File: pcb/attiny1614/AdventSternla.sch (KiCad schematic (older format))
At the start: 15 parts, among them J1 5V In, J2 GPIO_C, J3 UPDI, J4 GPIO_A, J5 NeoPixel, J6 GPIO_A, J7 GPIO_B, U1 ATTINY1614

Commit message: Schematic is done and started the layout
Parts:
- removed C3: 1000μF 16V, symbol CP
- removed J1: 5V In, symbol Conn_01x02_Female
- removed J4: GPIO_A, symbol Conn_01x03_Female
- removed J5: NeoPixel, symbol Conn_01x03_Male
- added C1: 2200μF 25V, Capacitors_ThroughHole:CP_Radial_D13.0mm_P5.00mm, symbol CP
- added J1: 5V In, Pin_Headers:Pin_Header_Straight_1x03_Pitch2.54mm, symbol Jack-DC
- added J6: NeoPixel Data, Pin_Headers:Pin_Header_Straight_1x02_Pitch2.54mm, symbol Conn_01x02_Male
- added J7: Power Out, Pin_Headers:Pin_Header_Straight_1x02_Pitch2.54mm, symbol Conn_01x02_Male
- C2: renamed from C1; footprint 0805 -> Capacitors_SMD:C_0805_HandSoldering
- C3: renamed from C2; footprint (none) -> Capacitors_SMD:C_0805_HandSoldering
- D1: value 5V Zener -> 5V6 Zener; footprint DO-214AA -> Diodes_SMD:D_SOT-23_ANK; Link https://www.reichelt.de/Ueberspannungs-schutzdioden/P6SMB-5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 -> https://www.digikey.de/scripts/DkSearch/dksus.dll?Detail&it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; MPN P6SMB 5,0A SMD -> BZX84-A5V6,215
- J2: footprint (none) -> Pin_Headers:Pin_Header_Straight_1x04_Pitch2.54mm
- J3: footprint (none) -> Pin_Headers:Pin_Header_Straight_2x03_Pitch2.54mm
- J4: renamed from J6; footprint (none) -> Pin_Headers:Pin_Header_Straight_1x03_Pitch2.54mm
- J5: renamed from J7; footprint (none) -> Pin_Headers:Pin_Header_Straight_1x04_Pitch2.54mm
- R1: footprint 1210 -> Resistors_SMD:R_1210_HandSoldering
- R2: footprint 0805 -> Resistors_SMD:R_0805_HandSoldering
- R3: footprint (none) -> Resistors_SMD:R_0805_HandSoldering
- U1: footprint (none) -> SMD_Packages:SOIC-14_N
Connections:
- net 5V: now also C1.1, J1.1, J7.1 (Pin_1)
- net GND: now also C1.2, J1.2, J6.2 (Pin_2), J7.2 (Pin_2)
- net NP_DATA: now reaches R3.2
- net NP_DATA: now also J6.1 (Pin_1)
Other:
- note added: "In System Programming Header - UPDI"
- note added: "The NoePixel has JST \nSM type connnectors"
- note removed: "In System Programming Header"
- moved on the sheet: C2, C3, D1, J2, J3, J4, J5, R1, R2, R3, U1

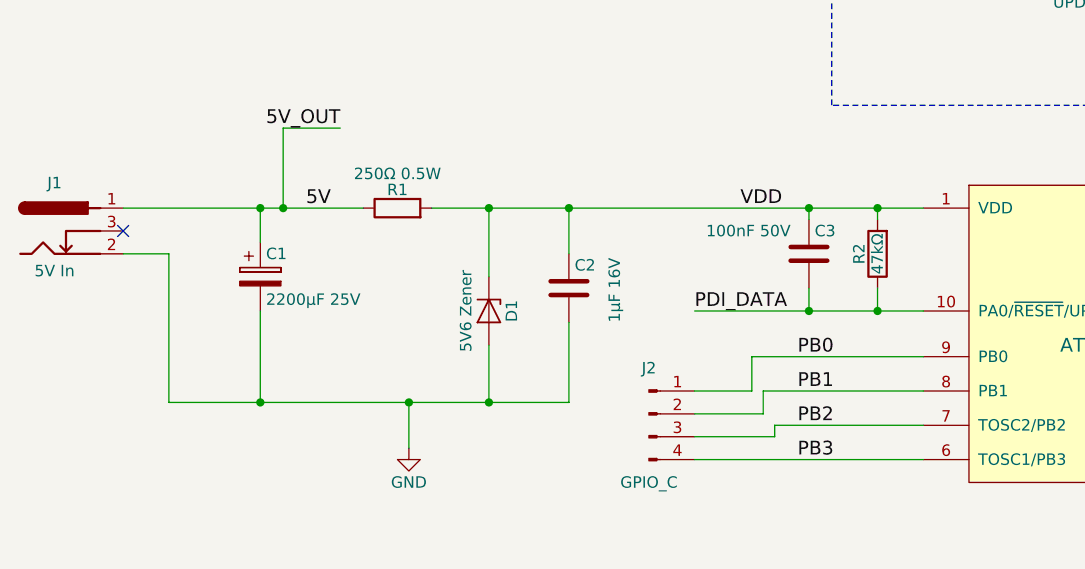
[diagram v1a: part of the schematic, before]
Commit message: Correction to power filtering
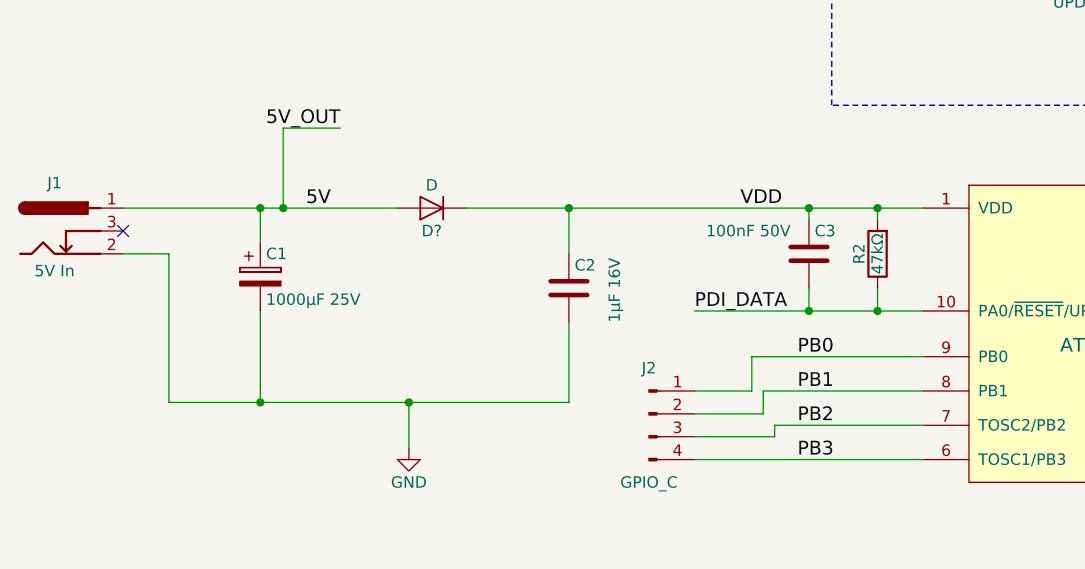
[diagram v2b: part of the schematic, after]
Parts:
- removed D1: 5V6 Zener, Diodes_SMD:D_SOT-23_ANK, symbol D_Zener
- removed R1: 250Ω 0.5W, Resistors_SMD:R_1210_HandSoldering, symbol R
- added D?: D, symbol D
- C1: value 2200μF 25V -> 1000μF 25V
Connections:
- net 5V: now also D?.2 (A)
- net VDD: now also D?.1 (K)
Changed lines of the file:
@@
 PA7
-$Comp
-L D_Zener D1
-U 1 1 59EF89E4
-P 2900 4300
-F 0 "D1" H 2900 4400 50  0000 C CNN
-F 1 "5V6 Zener" H 2900 4200 50  0000 C CNN
-F 2 "Diodes_SMD:D_SOT-23_ANK" H 2900 4300 50  0001 C CNN
-F 3 "http://cdn-reichelt.de/documents/datenblatt/A400/SMBJ_LITTELFUSE_DATASHEET.pdf" H 2900 4300 50  0001 C CNN
-F 4 "BZX84-A5V6,215" H 2900 4300 60  0001 C CNN "MPN"
-F 5 "https://www.digikey.de/scripts/DkSearch/dksus.dll?Detail&itemSeq=242065975&uq=636445409310237522" H 2900 4300 60  0001 C CNN "Link"
-	1    2900 4300
-	0    1    1    0
-$EndComp
-$Comp
-L R R1
-U 1 1 59EF8B11
-P 2500 3850
-F 0 "R1" V 2580 3850 50  0000 C CNN
-F 1 "250Ω 0.5W" V 2650 3850 50  0000 C CNN
-F 2 "Resistors_SMD:R_1210_HandSoldering" V 2430 3850 50  0001 C CNN
-F 3 "" H 2500 3850 50  0001 C CNN
-F 4 "ERJ-14NF2550U" H 2500 3850 60  0001 C CNN "MPN"
-F 5 "https://www.digikey.de/product-detail/de/panasonic-electronic-components/ERJ-14NF2550U/P255AACT-ND/384668" H 2500 3850 60  0001 C CNN "Link"
-	1    2500 3850
-	0    -1   -1   0
-$EndComp
 $Comp
 L Conn_01x04_Male J5
@@
 P 1900 4150
 F 0 "C1" H 1925 4250 50  0000 L CNN
-F 1 "2200μF 25V" H 1925 4050 50  0000 L CNN
+F 1 "1000μF 25V" H 1925 4050 50  0000 L CNN
 F 2 "Capacitors_ThroughHole:CP_Radial_D13.0mm_P5.00mm" H 1938 4000 50  0001 C CNN
 F 3 "" H 1900 4150 50  0001 C CNN
@@
 $EndComp
 Wire Wire Line
-	3800 4300 4800 4300
+	3800 4300 4300 4300
+Wire Wire Line
+	4300 4300 4600 4300
+Wire Wire Line
+	4600 4300 4800 4300
 Wire Wire Line
 	4600 4300 4600 4200
-Wire Wire Line
-	4600 3850 4600 3900
 Wire Wire Line
 	5600 5550 5600 5250
 Connection ~ 4600 4300
-Connection ~ 4600 3850
 Wire Wire Line
 	5200 2650 4750 2650
@@
 	6450 4750 7300 4750
 Wire Wire Line
-	2900 4150 2900 3850
-Wire Wire Line
-	2900 4700 2900 4450
-Wire Wire Line
-	1300 3850 2350 3850
-Wire Wire Line
-	2650 3850 4800 3850
-Connection ~ 2900 3850
+	1300 3850 1900 3850
+Wire Wire Line
+	1900 3850 2000 3850
+Wire Wire Line
+	2000 3850 2500 3850
 Wire Wire Line
 	4100 4650 4800 4650
 Wire Wire Line
 	4800 4950 3800 4950
-Wire Wire Line
-	4300 3850 4300 3900
-Connection ~ 4300 3850
 Wire Wire Line
 	4300 4200 4300 4300
@@
 Wire Wire Line
 	3250 3850 3250 4050
-Connection ~ 3250 3850
 Wire Wire Line
 	3250 4700 3250 4350
@@
 	1900 4300 1900 4700
 Wire Wire Line
-	1500 4700 3250 4700
+	1500 4700 1900 4700
+Wire Wire Line
+	1900 4700 2550 4700
+Wire Wire Line
+	2550 4700 3250 4700
 Wire Wire Line
 	2550 4700 2550 4900
 Connection ~ 1900 4700
 Connection ~ 2550 4700
-Connection ~ 2900 4700
 $Comp
 L Jack-DC J1
@@
 Text Notes 8400 2050 0    100  ~ 0
 NeoPixel
+$Comp
+L D D?
+U 1 1 59F5F260
+P 2650 3850
+F 0 "D?" H 2650 3950 50  0000 C CNN
+F 1 "D" H 2650 3750 50  0000 C CNN
+F 2 "" H 2650 3850 50  0001 C CNN
+F 3 "" H 2650 3850 50  0001 C CNN
+	1    2650 3850
+	-1   0    0    1
+$EndComp
+Wire Wire Line
+	2800 3850 3250 3850
+Wire Wire Line
+	3250 3850 4300 3850
+Wire Wire Line
+	4300 3850 4600 3850
+Wire Wire Line
+	4600 3850 4800 3850
+Connection ~ 3250 3850
+Wire Wire Line
+	4300 3900 4300 3850
+Connection ~ 4300 3850
+Wire Wire Line
+	4600 3900 4600 3850
+Connection ~ 4600 3850
 $EndSCHEMATC

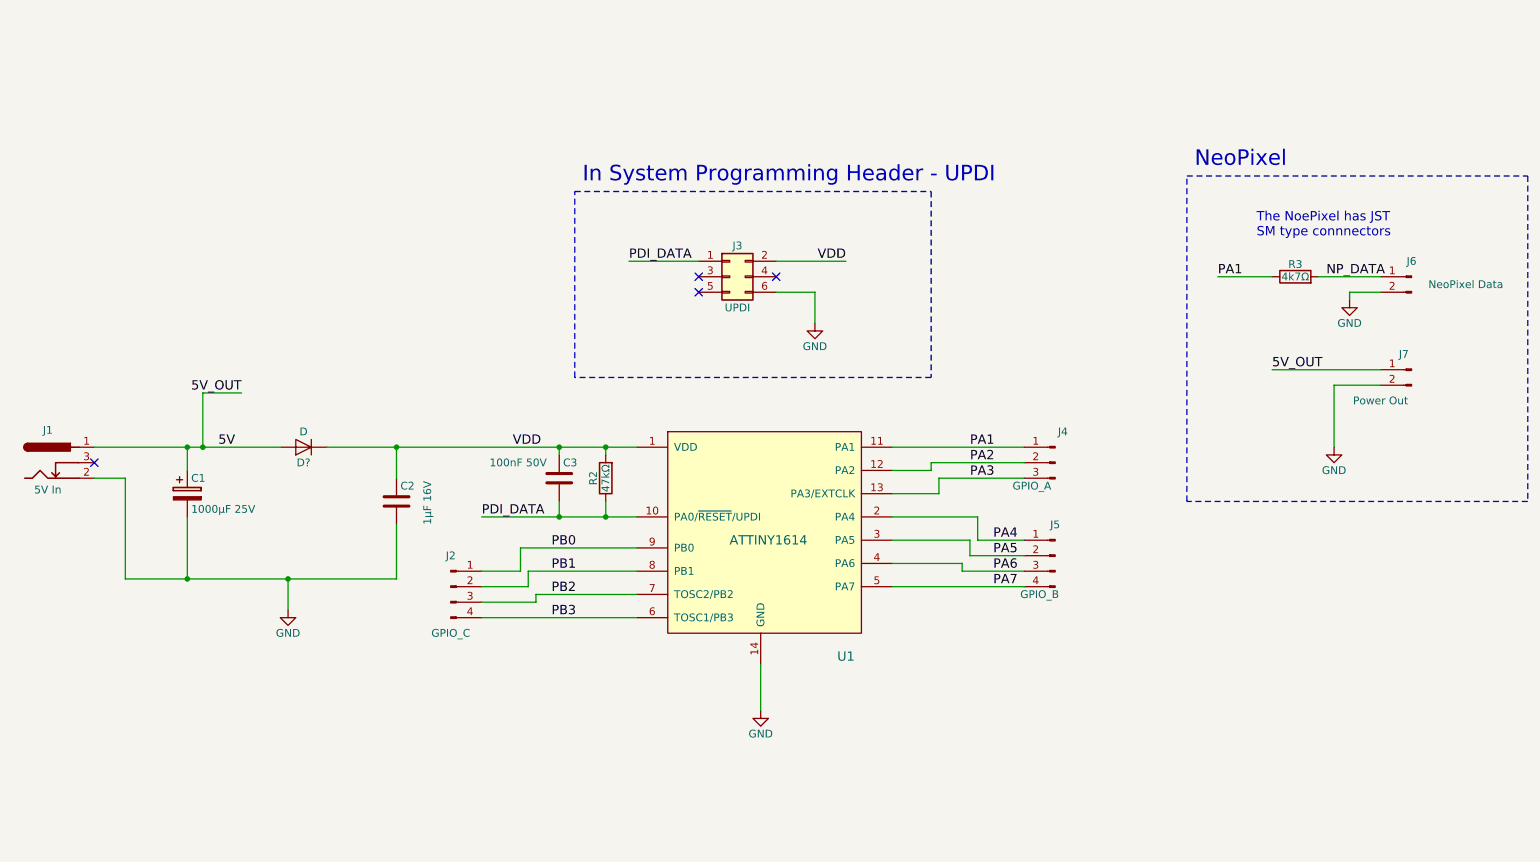
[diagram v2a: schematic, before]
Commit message: Annotated the changes to the power filtering
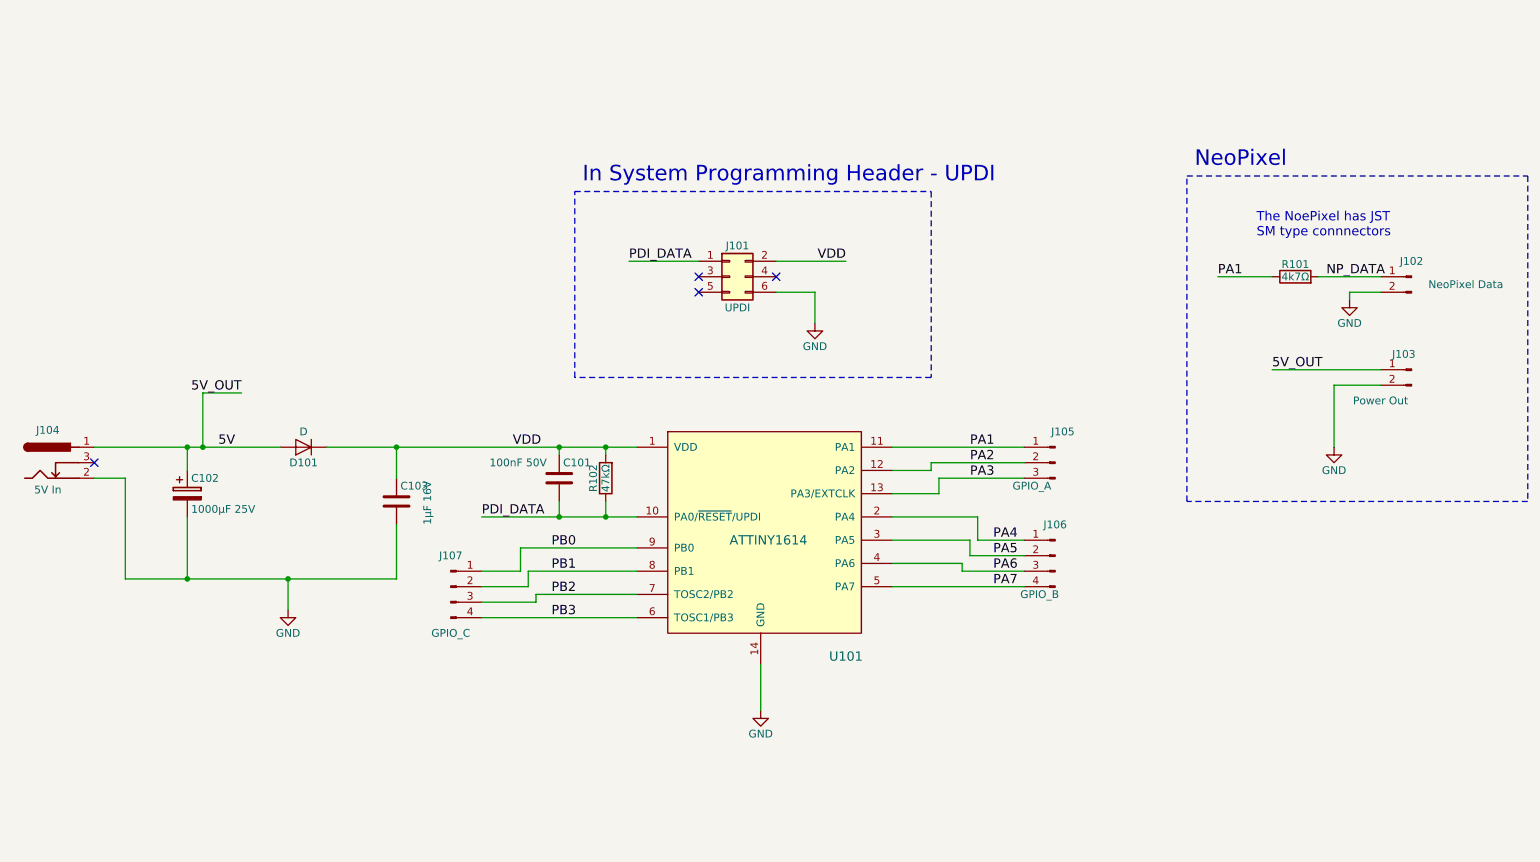
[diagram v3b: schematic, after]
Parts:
- gave numbers to parts that had none: 1
- renumbered C3 to C101, C1 to C102, C2 to C103, J3 to J101, J6 to J102, J7 to J103, J1 to J104, J4 to J105, J5 to J106, J2 to J107, R3 to R101, R2 to R102, U1 to U101
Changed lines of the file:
@@
 $EndDescr
 $Comp
-L ATTINY1614 U1
+L ATTINY1614 U101
 U 1 1 59EF6A42
 P 5600 4400
-F 0 "U1" H 6150 3600 60  0000 C CNN
+F 0 "U101" H 6150 3600 60  0000 C CNN
 F 1 "ATTINY1614" H 5650 4350 60  0000 C CNN
 F 2 "SMD_Packages:SOIC-14_N" H 5450 4450 60  0001 C CNN
@@
 $EndComp
 $Comp
-L R R2
+L R R102
 U 1 1 59EF6A7A
 P 4600 4050
-F 0 "R2" V 4680 4050 50  0000 C CNN
+F 0 "R102" V 4680 4050 50  0000 C CNN
 F 1 "47kΩ" V 4600 4050 50  0000 C CNN
 F 2 "Resistors_SMD:R_0805_HandSoldering" V 4530 4050 50  0001 C CNN
@@
 $EndComp
 $Comp
-L Conn_02x03_Odd_Even J3
+L Conn_02x03_Odd_Even J101
 U 1 1 59EF854F
 P 5400 2750
-F 0 "J3" H 5450 2950 50  0000 C CNN
+F 0 "J101" H 5450 2950 50  0000 C CNN
 F 1 "UPDI" H 5450 2550 50  0000 C CNN
 F 2 "Pin_Headers:Pin_Header_Straight_2x03_Pitch2.54mm" H 5400 2750 50  0001 C CNN
@@
 PA7
 $Comp
-L Conn_01x04_Male J5
+L Conn_01x04_Male J106
 U 1 1 59EF8DC0
 P 7500 4550
-F 0 "J5" H 7500 4750 50  0000 C CNN
+F 0 "J106" H 7500 4750 50  0000 C CNN
 F 1 "GPIO_B" H 7600 4300 50  0000 C CNN
 F 2 "Pin_Headers:Pin_Header_Straight_1x04_Pitch2.54mm" H 7500 4550 50  0001 C CNN
@@
 $EndComp
 $Comp
-L Conn_01x03_Male J4
+L Conn_01x03_Male J105
 U 1 1 59EF8E2B
 P 7500 3950
-F 0 "J4" H 7450 4150 50  0000 C CNN
+F 0 "J105" H 7450 4150 50  0000 C CNN
 F 1 "GPIO_A" H 7650 3800 50  0000 C CNN
 F 2 "Pin_Headers:Pin_Header_Straight_1x03_Pitch2.54mm" H 7500 3950 50  0001 C CNN
@@
 $EndComp
 $Comp
-L Conn_01x04_Male J2
+L Conn_01x04_Male J107
 U 1 1 59EF90A2
 P 3600 4750
-F 0 "J2" H 3600 4950 50  0000 C CNN
+F 0 "J107" H 3600 4950 50  0000 C CNN
 F 1 "GPIO_C" H 3600 4450 50  0000 C CNN
 F 2 "Pin_Headers:Pin_Header_Straight_1x04_Pitch2.54mm" H 3600 4750 50  0001 C CNN
@@
 PB3
 $Comp
-L C C3
+L C C101
 U 1 1 59EF9591
 P 4300 4050
-F 0 "C3" H 4325 4150 50  0000 L CNN
+F 0 "C101" H 4325 4150 50  0000 L CNN
 F 1 "100nF 50V" H 3850 4150 50  0000 L CNN
 F 2 "Capacitors_SMD:C_0805_HandSoldering" H 4338 3900 50  0001 C CNN
@@
 $EndComp
 $Comp
-L C C2
+L C C103
 U 1 1 59EF980D
 P 3250 4200
-F 0 "C2" H 3275 4300 50  0000 L CNN
+F 0 "C103" H 3275 4300 50  0000 L CNN
 F 1 "1μF 16V" V 3450 4050 50  0000 L CNN
 F 2 "Capacitors_SMD:C_0805_HandSoldering" H 3288 4050 50  0001 C CNN
@@
 $EndComp
 $Comp
-L R R3
+L R R101
 U 1 1 59EFA380
 P 9050 2750
-F 0 "R3" V 9130 2750 50  0000 C CNN
+F 0 "R101" V 9130 2750 50  0000 C CNN
 F 1 "4k7Ω" V 9050 2750 50  0000 C CNN
 F 2 "Resistors_SMD:R_0805_HandSoldering" V 8980 2750 50  0001 C CNN
@@
 The NoePixel has JST \nSM type connnectors
 $Comp
-L Conn_01x02_Male J6
+L Conn_01x02_Male J102
 U 1 1 59F0DA81
 P 9800 2750
-F 0 "J6" H 9800 2850 50  0000 C CNN
+F 0 "J102" H 9800 2850 50  0000 C CNN
 F 1 "NeoPixel Data" H 9450 2700 50  0000 C CNN
 F 2 "Pin_Headers:Pin_Header_Straight_1x02_Pitch2.54mm" H 9800 2750 50  0001 C CNN
@@
 $EndComp
 $Comp
-L Conn_01x02_Male J7
+L Conn_01x02_Male J103
 U 1 1 59F0DC96
 P 9800 3350
-F 0 "J7" H 9850 3450 50  0000 C CNN
+F 0 "J103" H 9850 3450 50  0000 C CNN
 F 1 "Power Out" H 10000 3150 50  0000 C CNN
 F 2 "Pin_Headers:Pin_Header_Straight_1x02_Pitch2.54mm" H 9800 3350 50  0001 C CNN
@@
 $EndComp
 $Comp
-L CP C1
+L CP C102
 U 1 1 59F0F869
 P 1900 4150
-F 0 "C1" H 1925 4250 50  0000 L CNN
+F 0 "C102" H 1925 4250 50  0000 L CNN
 F 1 "1000μF 25V" H 1925 4050 50  0000 L CNN
 F 2 "Capacitors_ThroughHole:CP_Radial_D13.0mm_P5.00mm" H 1938 4000 50  0001 C CNN
@@
 $EndComp
 Wire Wire Line
-	3800 4300 4300 4300
-Wire Wire Line
-	4300 4300 4600 4300
-Wire Wire Line
-	4600 4300 4800 4300
+	3800 4300 4800 4300
 Wire Wire Line
 	4600 4300 4600 4200
@@
 	6450 4750 7300 4750
 Wire Wire Line
-	1300 3850 1900 3850
-Wire Wire Line
-	1900 3850 2000 3850
-Wire Wire Line
-	2000 3850 2500 3850
+	1300 3850 2500 3850
 Wire Wire Line
 	4100 4650 4800 4650
@@
 	1900 4300 1900 4700
 Wire Wire Line
-	1500 4700 1900 4700
-Wire Wire Line
-	1900 4700 2550 4700
-Wire Wire Line
-	2550 4700 3250 4700
+	1500 4700 3250 4700
 Wire Wire Line
 	2550 4700 2550 4900
@@
 Connection ~ 2550 4700
 $Comp
-L Jack-DC J1
+L Jack-DC J104
 U 1 1 59F100E4
 P 1000 3950
-F 0 "J1" H 1000 4160 50  0000 C CNN
+F 0 "J104" H 1000 4160 50  0000 C CNN
 F 1 "5V In" H 1000 3775 50  0000 C CNN
 F 2 "Pin_Headers:Pin_Header_Straight_1x03_Pitch2.54mm" H 1050 3910 50  0001 C CNN
@@
 NeoPixel
 $Comp
-L D D?
+L D D101
 U 1 1 59F5F260
 P 2650 3850
-F 0 "D?" H 2650 3950 50  0000 C CNN
+F 0 "D101" H 2650 3950 50  0000 C CNN
 F 1 "D" H 2650 3750 50  0000 C CNN
 F 2 "" H 2650 3850 50  0001 C CNN
@@
 $EndComp
 Wire Wire Line
-	2800 3850 3250 3850
-Wire Wire Line
-	3250 3850 4300 3850
-Wire Wire Line
-	4300 3850 4600 3850
-Wire Wire Line
-	4600 3850 4800 3850
+	2800 3850 4800 3850
 Connection ~ 3250 3850
 Wire Wire Line

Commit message: Initial layout completed
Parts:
- C102: footprint Capacitors_ThroughHole:CP_Radial_D13.0mm_P5.00mm -> advent_sternla:CP_Radial_L21.0mm_D13.0mm_P5.00mm_Horizontal
- D101: value D -> 1N4148WSTR; footprint (none) -> Diodes_SMD:D_SOD-323; ConradPN (none) -> Value; Label (none) -> Value; MPN (none) -> 1N4148WSTR
- J101: footprint Pin_Headers:Pin_Header_Straight_2x03_Pitch2.54mm -> advent_sternla:PRG_TC2030-IDC-NL
- J104: footprint Pin_Headers:Pin_Header_Straight_1x03_Pitch2.54mm -> advent_sternla:CONN_PWR_JACK_1_3X3_5MM_SOLDER
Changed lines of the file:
@@
 F 0 "J101" H 5450 2950 50  0000 C CNN
 F 1 "UPDI" H 5450 2550 50  0000 C CNN
-F 2 "Pin_Headers:Pin_Header_Straight_2x03_Pitch2.54mm" H 5400 2750 50  0001 C CNN
+F 2 "advent_sternla:PRG_TC2030-IDC-NL" H 5400 2750 50  0001 C CNN
 F 3 "" H 5400 2750 50  0001 C CNN
 	1    5400 2750
@@
 P 3250 4200
 F 0 "C103" H 3275 4300 50  0000 L CNN
-F 1 "1μF 16V" V 3450 4050 50  0000 L CNN
+F 1 "1μF 16V" H 3100 4100 50  0000 L CNN
 F 2 "Capacitors_SMD:C_0805_HandSoldering" H 3288 4050 50  0001 C CNN
 F 3 "" H 3250 4200 50  0001 C CNN
@@
 F 0 "C102" H 1925 4250 50  0000 L CNN
 F 1 "1000μF 25V" H 1925 4050 50  0000 L CNN
-F 2 "Capacitors_ThroughHole:CP_Radial_D13.0mm_P5.00mm" H 1938 4000 50  0001 C CNN
+F 2 "advent_sternla:CP_Radial_L21.0mm_D13.0mm_P5.00mm_Horizontal" H 1938 4000 50  0001 C CNN
 F 3 "" H 1900 4150 50  0001 C CNN
 	1    1900 4150
@@
 F 0 "J104" H 1000 4160 50  0000 C CNN
 F 1 "5V In" H 1000 3775 50  0000 C CNN
-F 2 "Pin_Headers:Pin_Header_Straight_1x03_Pitch2.54mm" H 1050 3910 50  0001 C CNN
+F 2 "advent_sternla:CONN_PWR_JACK_1_3X3_5MM_SOLDER" H 1050 3910 50  0001 C CNN
 F 3 "http://www.cui.com/product/resource/pj-031dh.pdf" H 1050 3910 50  0001 C CNN
 F 4 "PJ-031DH" H 1000 3950 60  0001 C CNN "MPN"
@@
 P 2650 3850
 F 0 "D101" H 2650 3950 50  0000 C CNN
-F 1 "D" H 2650 3750 50  0000 C CNN
-F 2 "" H 2650 3850 50  0001 C CNN
-F 3 "" H 2650 3850 50  0001 C CNN
+F 1 "1N4148WSTR" H 2650 3750 50  0000 C CNN
+F 2 "Diodes_SMD:D_SOD-323" H 2650 3850 50  0001 C CNN
+F 3 "http://www.smc-diodes.com/propdf/1N4148WS%20N0572%20REV.B.pdf" H 2650 3850 50  0001 C CNN
+F 4 "1N4148WSTR" H 2650 3850 60  0001 C CNN "MPN"
+F 5 "Value" H 2650 3850 60  0001 C CNN "ConradPN"
+F 6 "Value" H 2650 3850 60  0001 C CNN "Label"
 	1    2650 3850
 	-1   0    0    1

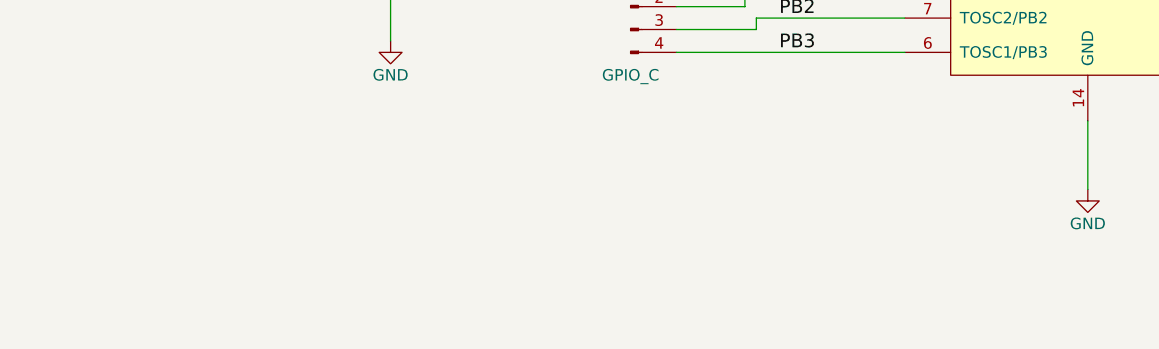
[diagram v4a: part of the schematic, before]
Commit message: Added some more nomenclature for the pin headers
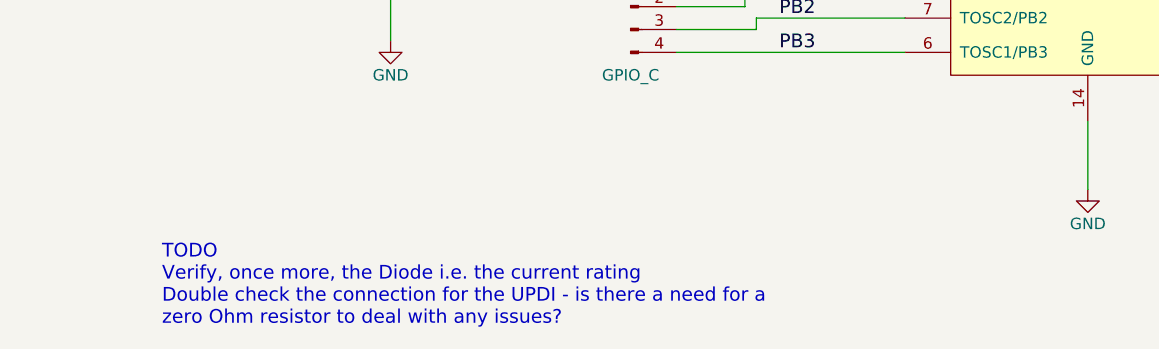
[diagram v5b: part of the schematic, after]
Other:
- note added: "TODO \nVerify, once more, the Diode i.e. the current rating\nDouble check the connection for the UPDI - is there a need for a \nzero Ohm resistor to deal with any issues?"
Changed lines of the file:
@@
 	4600 3900 4600 3850
 Connection ~ 4600 3850
+Text Notes 1550 6150 0    60   ~ 0
+TODO \nVerify, once more, the Diode i.e. the current rating\nDouble check the connection for the UPDI - is there a need for a \nzero Ohm resistor to deal with any issues?
 $EndSCHEMATC
